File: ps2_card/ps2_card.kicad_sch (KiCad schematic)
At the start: 16 parts, among them J1 Conn1, J2 Mouse, J3 Keyboard, U1 HT6542B, U2 74HCT04

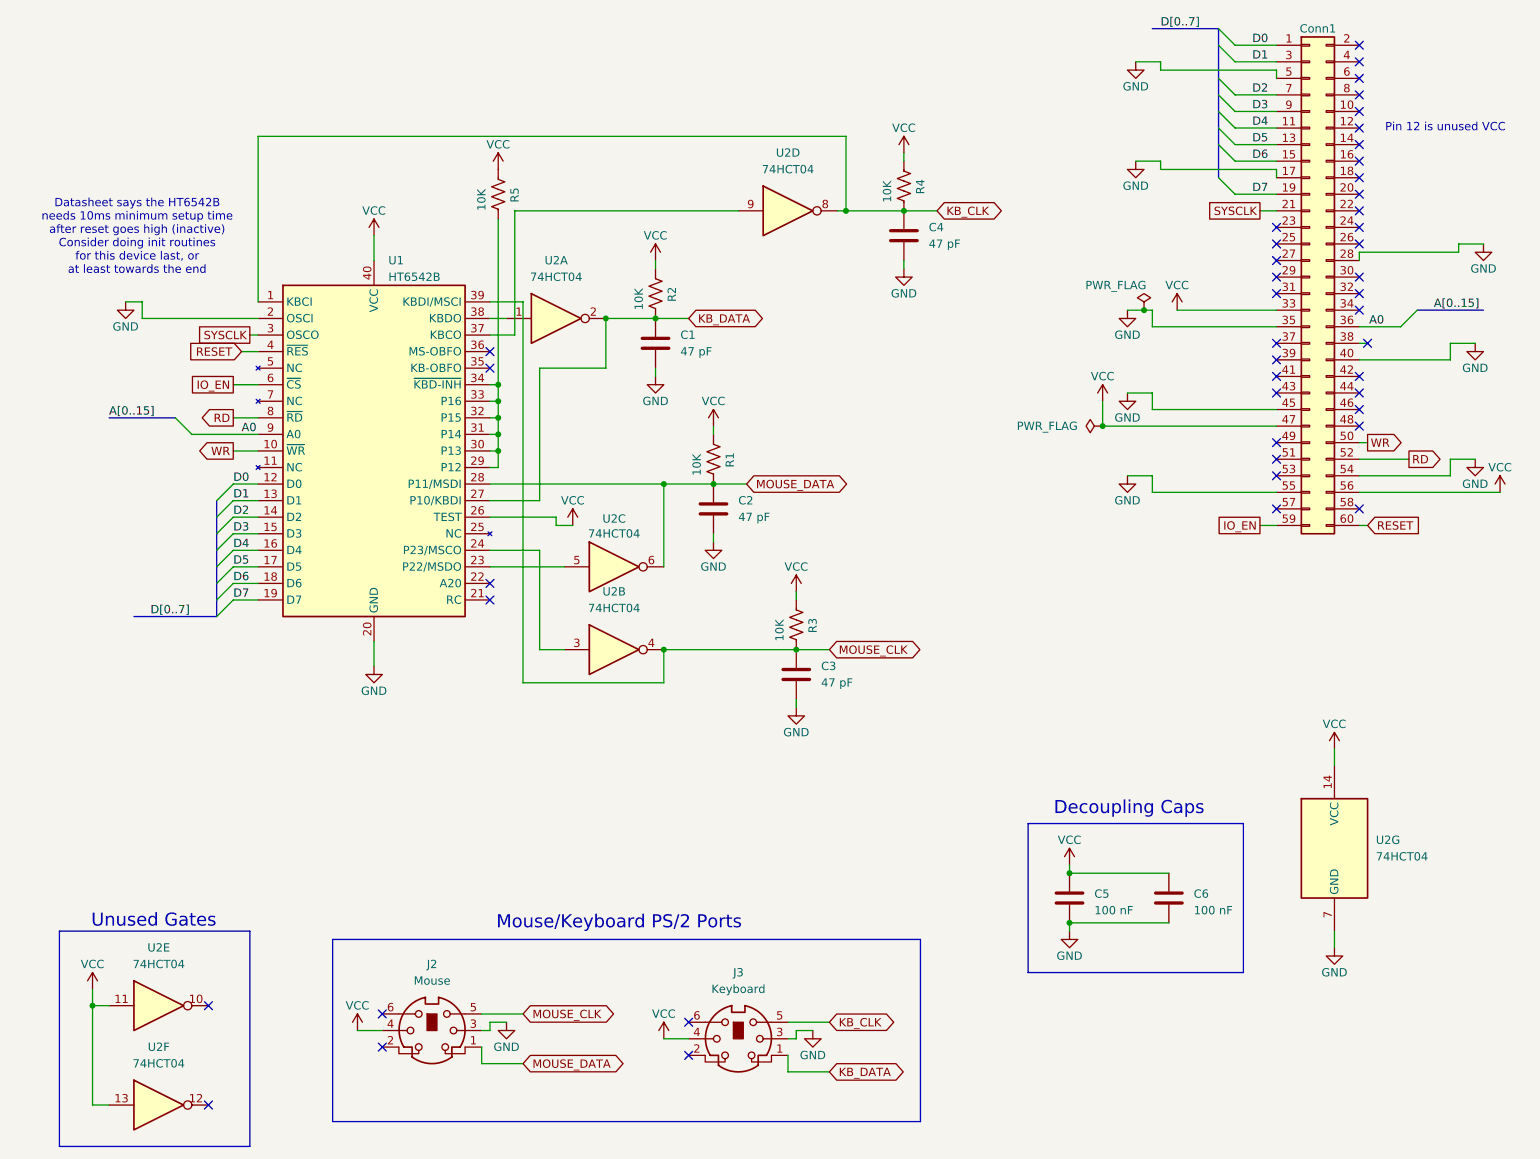
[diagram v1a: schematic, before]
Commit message: Replaced 74xx04's with 74xx06's in order for the ps/2 device to be able to properly send data/clock
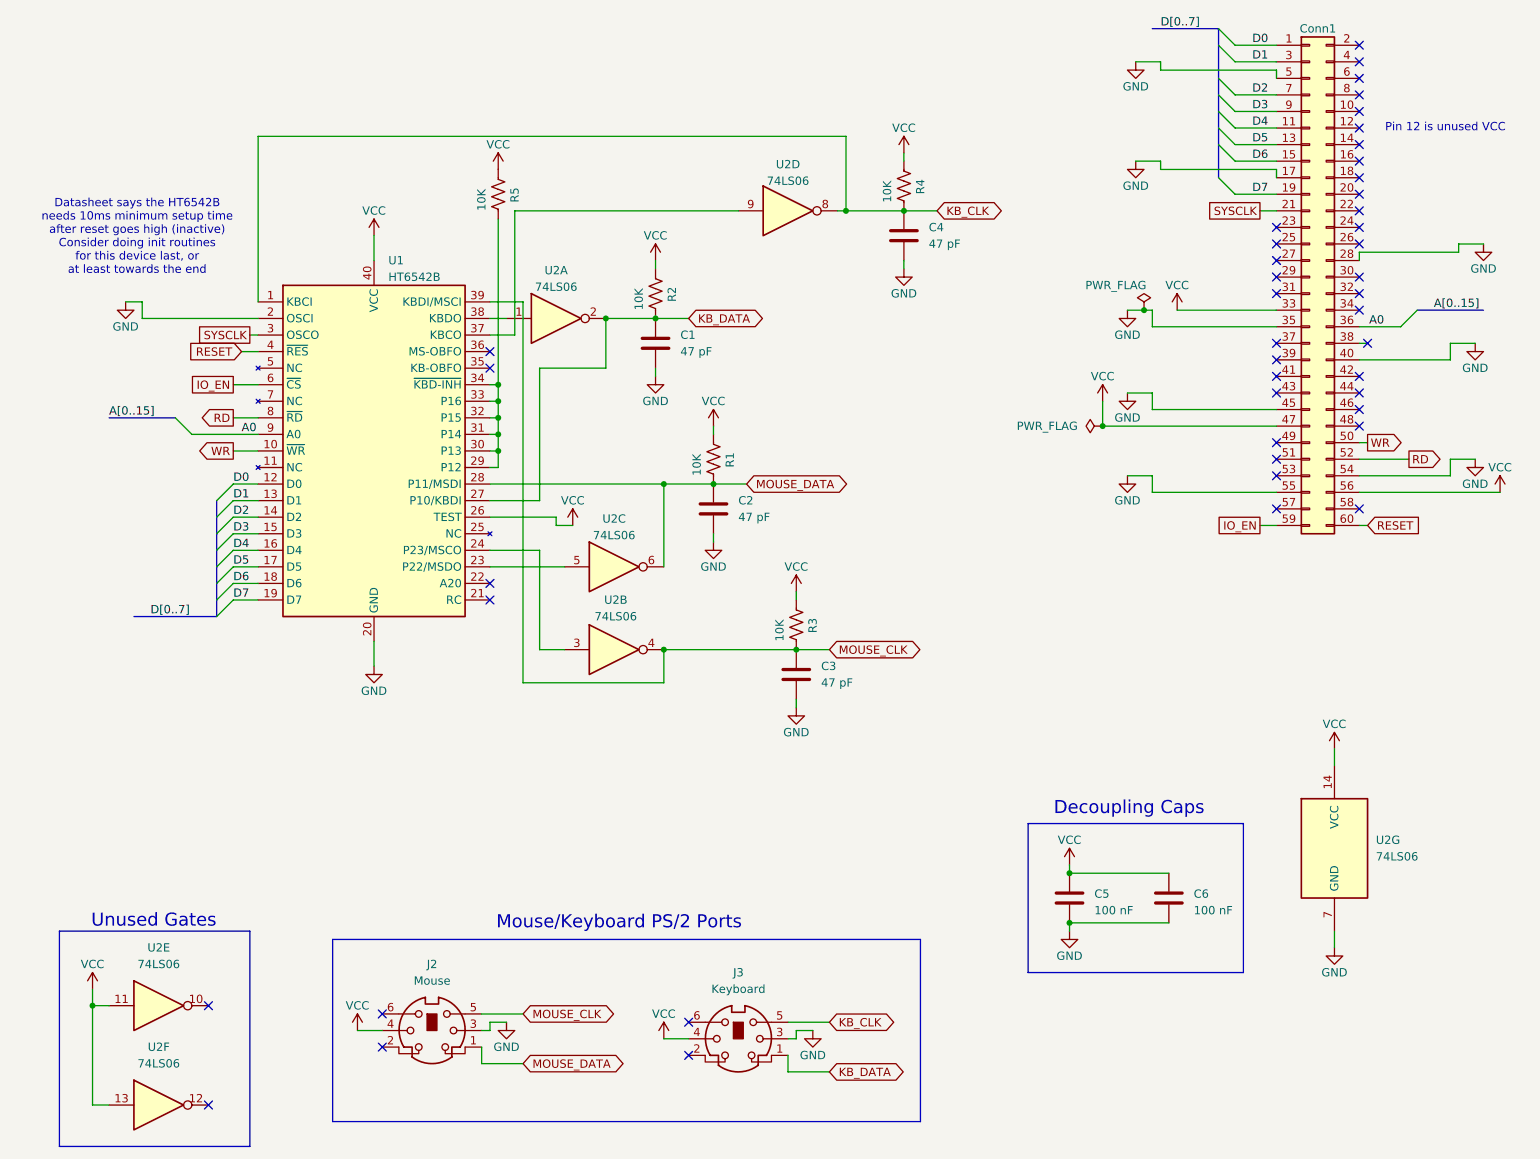
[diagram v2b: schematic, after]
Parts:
- removed U2: 74HCT04, Package_DIP:DIP-14_W7.62mm, symbol 74xx:74HCT04
- added U2: 74LS06, Package_DIP:DIP-14_W7.62mm, symbol 74xx:74LS06
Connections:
- net GND: now also U2.7 (GND)
- net KB_CLK: now also U2.8
- net KB_DATA: now also U2.2
- net MOUSE_CLK: now also U2.4
- net MOUSE_DATA: now also U2.6
- net VCC: now also U2.11, U2.13, U2.14 (VCC)
- net at U1.37 (KBCO): now also U2.9
- net at U1.24 (P23/MSCO): now also U2.3
- net at U1.23 (P22/MSDO): now also U2.5
- net at U1.38 (KBDO): now also U2.1
